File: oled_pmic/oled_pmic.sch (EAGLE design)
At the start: 11 parts, among them J1 I_sense, J2 VCC, J4 GND, Q1 N-CHANNEL-MOSFETSOT23-3, U1 AL5801W6-7

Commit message: start oled pmic module
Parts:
- removed C1: 0.1uF, scono:CAP0603-CAP
- removed D1, D2: (no value), scono:LED0603
- removed J3: (no value), scono:CONN_03
- removed J4: GND, scono:CONN_02
- added C2, C3, C4, C5, C8: 100nF, scono:CAP0402-CAP
- added C6, C7: 18pF, scono:CAP0402-CAP
- added D3: (no value), scono:LED0603
- added D4: RED, scono:LED0603
- added J10, J6: GND, scono:CONN_02
- added J12: BURNIN, scono:BURNIN
- added J5, J9: VCC, scono:CONN_02
- added J7: UART, scono:CONN_02
- added J8: FTDI, scono:CONN_06NO_SILK_FEMALE_PTH
- added Q2, Q3, Q4: N-CHANNEL-MOSFETSOT23-3, scono:N-CHANNEL-MOSFETSOT23-3
- added R10, R11, R14, R15, R18, R19, R6, R7: 100k, scono:R-US_R0402
- added R12, R16, R8: 1.6R, scono:R-US_0603
- added R13, R17, R9: 52.5k, scono:R-US_0603
- added R3: 10k, scono:R-US_R0402
- added R4, R5: 500R, scono:R-US_R0402
- added SW1: BTN-PTS810, scono:BTN-PTS810
- added TP1: TEST_POINTTHRU, scono:TEST_POINTTHRU
- added U2: LM340MPX-5.0230, scono:LM340MPX-5.0230
- added U3: ATMEGA328P-AUR, scono:ATMEGA328P-AUR
- added U4, U5, U6: AL5801W6-7, scono:AL5801W6-7
- added Y1: 16MHz, scono:CRYSTAL_SMOL
- J1: value I_sense -> (none); device scono:CONN_02 -> scono:CONN_04
- J2: value VCC -> (none); device scono:CONN_02 -> scono:CONN_04
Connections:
- removed net BIAS: J3.2, Q1.D, R2.1, U1.BIAS
- removed net FB: J3.1, R1.2, U1.FB, U1.REXT
- removed net N$2: D1.A, D2.C
- removed net N$3: J1.1, U1.OUT
- removed net N$4: D1.C, J1.2
- removed net PWM: J3.3, Q1.G
- new net 5V: C3.2, C4.2, C5.2, J12.VCC, J8.4, R3.2, R5.1, TP1.P$1, U2.5V, U3.AVCC, U3.VCC
- new net ADC0: R6.1, R7.2, U3.PC0(ADC0/PCINT8)
- new net ADC1: R10.1, R11.2, U3.PC1(ADC1/PCINT9)
- new net ADC2: R14.1, R15.2, U3.PC2(ADC2/PCINT10)
- new net ADC3: R18.1, R19.2, U3.PC3(ADC3/PCINT11)
- new net BIAS1: Q1.D, R2.1, U1.BIAS
- new net BIAS2: Q2.D, R9.1, U4.BIAS
- new net BIAS3: Q3.D, R13.1, U5.BIAS
- new net BIAS4: Q4.D, R17.1, U6.BIAS
- new net CAT1: J2.1, R6.2, U1.OUT
- new net CAT2: J2.2, R10.2, U4.OUT
- new net CAT3: J2.3, R14.2, U5.OUT
- new net CAT4: J2.4, R18.2, U6.OUT
- new net CTS: J8.5
- new net FB1: R1.2, U1.FB, U1.REXT
- new net FB2: R8.2, U4.FB, U4.REXT
- new net FB3: R12.2, U5.FB, U5.REXT
- new net FB4: R16.2, U6.FB, U6.REXT
- new net GPIO0: R4.2, U3.PD2(INT0/PCINT18)
- new net GPIO1: U3.PD3(PCINT19/OC2B/INT1)
- new net GPIO2: U3.PD4(PCINT20/XCK/T0)
- new net GPIO3: U3.PD5(PCINT21/OC0B/T1)
- new net GPIO4: U3.PD6(PCINT22/OC0A/AIN0)
- new net GPIO5: U3.PD7(PCINT23/AIN1)
- new net GPIO6: U3.PB0(PCINT0/CLKO/ICP1)
- new net GPIO7: U3.PB1(PCINT1/OC1A)
- new net MISO: J12.MISO, U3.PB4(PCINT4/MISO)
- new net MOSI: J12.MOSI, U3.PB3(PCINT3/OC2A/MOSI)
- new net N$1: D3.A, R4.1
- new net N$5: D4.A, R5.2
- new net N$6: C8.2, J8.1
- new net PWM1: Q1.G
- new net PWM2: Q2.G
- new net PWM3: Q3.G
- new net PWM4: Q4.G
- new net RST: C8.1, J12.RST, R3.1, SW1.B, U3.PC6(!RESET!/PCINT14)
- new net RX: J7.1, J8.3, U3.PD0(RXD/PCINT16)
- new net SCK: J12.SCK, U3.PB5(SCK/PCINT5)
- new net SCL: U3.PC5(ADC5/SCL/PCINT13)
- new net SDA: U3.PC4(ADC4/SDA/PCINT12)
- new net SS: U3.PB2(PCINT2/!SS!/OC1B)
- new net TX: J7.2, J8.2, U3.PD1(TXD/PCINT17)
- new net XTAL1: C6.1, U3.PB6(PCINT6/XTAL1/TOSC1), Y1.B
- new net XTAL2: C7.1, U3.PB7(PCINT7/XTAL2/TOSC2), Y1.A
- net GND: now also C2.1, C3.1, C4.1, C5.1, C6.2, C7.2, D3.C, D4.C, J10.1, J10.2, J12.GND, J6.1, J6.2, J8.6, Q2.S@2, Q3.S@2, Q4.S@2, R11.1, R12.1, R15.1, R16.1, R19.1, R7.1, R8.1, SW1.A, U2.GND, U3.GND, U4.GND, U5.GND, U6.GND; no longer C1.1, J4.1, J4.2
- net VCC: now also C2.2, J1.1, J1.2, J1.3, J1.4, J5.1, J5.2, J9.1, J9.2, R13.2, R17.2, R9.2, U2.VIN; no longer C1.2, D2.A, J2.1, J2.2

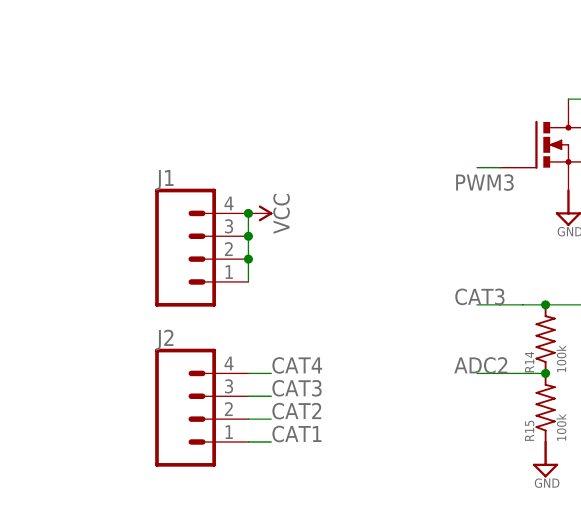
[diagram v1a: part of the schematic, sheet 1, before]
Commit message: finish oled module
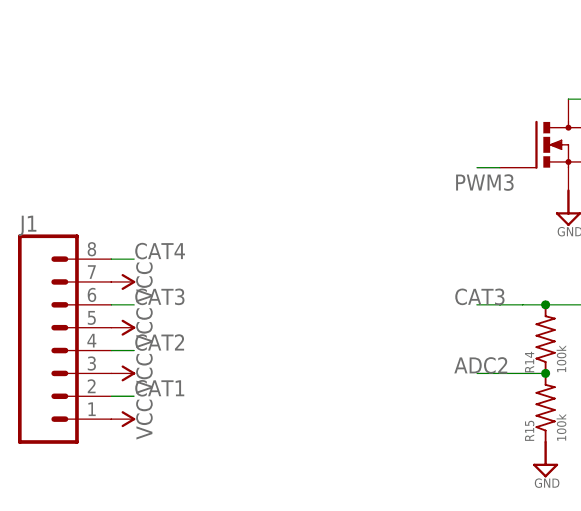
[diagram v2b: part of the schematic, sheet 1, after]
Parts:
- removed J2: (no value), scono:CONN_04
- J1: device scono:CONN_04 -> scono:CONN_08"
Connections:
- removed net GPIO1: U3.PD3(PCINT19/OC2B/INT1)
- removed net GPIO3: U3.PD5(PCINT21/OC0B/T1)
- removed net GPIO4: U3.PD6(PCINT22/OC0A/AIN0)
- removed net GPIO7: U3.PB1(PCINT1/OC1A)
- net CAT1: now also J1.2; no longer J2.1
- net CAT2: now also J1.4; no longer J2.2
- net CAT3: now also J1.6; no longer J2.3
- net CAT4: now also J1.8; no longer J2.4
- net PWM1: now also U3.PB1(PCINT1/OC1A)
- net PWM2: now also U3.PD6(PCINT22/OC0A/AIN0)
- net PWM3: now also U3.PD5(PCINT21/OC0B/T1)
- net PWM4: now also U3.PD3(PCINT19/OC2B/INT1)
- net VCC: now also J1.5, J1.7; no longer J1.2, J1.4
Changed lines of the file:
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@@
 <part name="SUPPLY24" library="scono" library_urn="urn:adsk.eagle:library:14850048" deviceset="GND" device=""/>
 <part name="TP1" library="scono" library_urn="urn:adsk.eagle:library:14850048" deviceset="TEST_POINT" device="THRU" package3d_urn="urn:adsk.eagle:package:14850798/1"/>
-<part name="J1" library="scono" library_urn="urn:adsk.eagle:library:14850048" deviceset="CONN_04" device="" package3d_urn="urn:adsk.eagle:package:38085/1"/>
-<part name="SUPPLY1" library="scono" library_urn="urn:adsk.eagle:library:14850048" deviceset="VCC" device=""/>
 <part name="R6" library="scono" library_urn="urn:adsk.eagle:library:14850048" deviceset="R-US_" device="R0402" package3d_urn="urn:adsk.eagle:package:14850590/3" value="100k"/>
 <part name="R7" library="scono" library_urn="urn:adsk.eagle:library:14850048" deviceset="R-US_" device="R0402" package3d_urn="urn:adsk.eagle:package:14850590/3" value="100k"/>
@@
 <part name="R19" library="scono" library_urn="urn:adsk.eagle:library:14850048" deviceset="R-US_" device="R0402" package3d_urn="urn:adsk.eagle:package:14850590/3" value="100k"/>
 <part name="SUPPLY33" library="scono" library_urn="urn:adsk.eagle:library:14850048" deviceset="GND" device=""/>
-<part name="J2" library="scono" library_urn="urn:adsk.eagle:library:14850048" deviceset="CONN_04" device="" package3d_urn="urn:adsk.eagle:package:38085/1"/>
+<part name="SUPPLY1" library="scono" library_urn="urn:adsk.eagle:library:14850048" deviceset="VCC" device=""/>
+<part name="SUPPLY34" library="scono" library_urn="urn:adsk.eagle:library:14850048" deviceset="VCC" device=""/>
+<part name="SUPPLY35" library="scono" library_urn="urn:adsk.eagle:library:14850048" deviceset="VCC" device=""/>
+<part name="SUPPLY36" library="scono" library_urn="urn:adsk.eagle:library:14850048" deviceset="VCC" device=""/>
+<part name="J1" library="scono" library_urn="urn:adsk.eagle:library:14850048" deviceset="CONN_08" device="&quot;" package3d_urn="urn:adsk.eagle:package:38138/1"/>
 </parts>
 <sheets>
@@
 <attribute name="VALUE" x="29.21" y="132.08" size="1.016" layer="96"/>
 </instance>
-<instance part="J1" gate="G$1" x="35.56" y="68.58" smashed="yes">
-<attribute name="VALUE" x="30.48" y="61.214" size="1.778" layer="96" font="vector"/>
-<attribute name="NAME" x="30.48" y="76.708" size="1.778" layer="95" font="vector"/>
-</instance>
-<instance part="SUPPLY1" gate="G$1" x="40.64" y="73.66" smashed="yes" rot="R270">
-<attribute name="VALUE" x="43.434" y="73.66" size="1.778" layer="96" rot="R270" align="bottom-center"/>
-</instance>
 <instance part="R6" gate="G$1" x="27.94" y="121.92" smashed="yes" rot="R90">
 <attribute name="NAME" x="26.67" y="116.84" size="1.016" layer="95" rot="R90"/>
@@
 <attribute name="VALUE" x="156.21" y="43.18" size="1.016" layer="96"/>
 </instance>
-<instance part="J2" gate="G$1" x="35.56" y="50.8" smashed="yes">
-<attribute name="VALUE" x="30.48" y="43.434" size="1.778" layer="96" font="vector"/>
-<attribute name="NAME" x="30.48" y="58.928" size="1.778" layer="95" font="vector"/>
+<instance part="SUPPLY1" gate="G$1" x="25.4" y="66.04" smashed="yes" rot="R270">
+<attribute name="VALUE" x="28.194" y="66.04" size="1.778" layer="96" rot="R270" align="bottom-center"/>
+</instance>
+<instance part="SUPPLY34" gate="G$1" x="25.4" y="60.96" smashed="yes" rot="R270">
+<attribute name="VALUE" x="28.194" y="60.96" size="1.778" layer="96" rot="R270" align="bottom-center"/>
+</instance>
+<instance part="SUPPLY35" gate="G$1" x="25.4" y="55.88" smashed="yes" rot="R270">
+<attribute name="VALUE" x="28.194" y="55.88" size="1.778" layer="96" rot="R270" align="bottom-center"/>
+</instance>
+<instance part="SUPPLY36" gate="G$1" x="25.4" y="50.8" smashed="yes" rot="R270">
+<attribute name="VALUE" x="28.194" y="50.8" size="1.778" layer="96" rot="R270" align="bottom-center"/>
+</instance>
+<instance part="J1" gate="G$1" x="20.32" y="58.42" smashed="yes">
+<attribute name="VALUE" x="15.24" y="45.974" size="1.778" layer="96" font="vector"/>
+<attribute name="NAME" x="15.24" y="71.628" size="1.778" layer="95" font="vector"/>
 </instance>
 </instances>
@@
 </segment>
 <segment>
-<pinref part="J1" gate="G$1" pin="4"/>
-<pinref part="SUPPLY1" gate="G$1" pin="VCC"/>
-<pinref part="J1" gate="G$1" pin="3"/>
-<wire x1="40.64" y1="73.66" x2="40.64" y2="71.12" width="0.1524" layer="91"/>
-<junction x="40.64" y="73.66"/>
-<pinref part="J1" gate="G$1" pin="2"/>
-<wire x1="40.64" y1="71.12" x2="40.64" y2="68.58" width="0.1524" layer="91"/>
-<junction x="40.64" y="71.12"/>
-<pinref part="J1" gate="G$1" pin="1"/>
-<wire x1="40.64" y1="68.58" x2="40.64" y2="66.04" width="0.1524" layer="91"/>
-<junction x="40.64" y="68.58"/>
-</segment>
-<segment>
 <pinref part="R9" gate="G$1" pin="2"/>
 <pinref part="SUPPLY5" gate="G$1" pin="VCC"/>
@@
 <pinref part="R17" gate="G$1" pin="2"/>
 <pinref part="SUPPLY30" gate="G$1" pin="VCC"/>
+</segment>
+<segment>
+<pinref part="SUPPLY1" gate="G$1" pin="VCC"/>
+<pinref part="J1" gate="G$1" pin="7"/>
+</segment>
+<segment>
+<pinref part="SUPPLY34" gate="G$1" pin="VCC"/>
+<pinref part="J1" gate="G$1" pin="5"/>
+</segment>
+<segment>
+<pinref part="SUPPLY35" gate="G$1" pin="VCC"/>
+<pinref part="J1" gate="G$1" pin="3"/>
+</segment>
+<segment>
+<pinref part="SUPPLY36" gate="G$1" pin="VCC"/>
+<pinref part="J1" gate="G$1" pin="1"/>
 </segment>
 </net>
@@
 </segment>
 <segment>
-<pinref part="J2" gate="G$1" pin="1"/>
-<wire x1="40.64" y1="48.26" x2="43.18" y2="48.26" width="0.1524" layer="91"/>
-<label x="43.18" y="48.26" size="1.778" layer="95"/>
+<wire x1="25.4" y1="53.34" x2="27.94" y2="53.34" width="0.1524" layer="91"/>
+<label x="27.94" y="53.34" size="1.778" layer="95"/>
+<pinref part="J1" gate="G$1" pin="2"/>
 </segment>
 </net>
@@
 </segment>
 <segment>
-<pinref part="J2" gate="G$1" pin="2"/>
-<wire x1="40.64" y1="50.8" x2="43.18" y2="50.8" width="0.1524" layer="91"/>
-<label x="43.18" y="50.8" size="1.778" layer="95"/>
+<wire x1="25.4" y1="58.42" x2="27.94" y2="58.42" width="0.1524" layer="91"/>
+<label x="27.94" y="58.42" size="1.778" layer="95"/>
+<pinref part="J1" gate="G$1" pin="4"/>
 </segment>
 </net>
@@
 </segment>
 <segment>
-<pinref part="J2" gate="G$1" pin="3"/>
-<wire x1="40.64" y1="53.34" x2="43.18" y2="53.34" width="0.1524" layer="91"/>
-<label x="43.18" y="53.34" size="1.778" layer="95"/>
+<wire x1="25.4" y1="63.5" x2="27.94" y2="63.5" width="0.1524" layer="91"/>
+<label x="27.94" y="63.5" size="1.778" layer="95"/>
+<pinref part="J1" gate="G$1" pin="6"/>
 </segment>
 </net>
@@
 </segment>
 <segment>
-<pinref part="J2" gate="G$1" pin="4"/>
-<wire x1="40.64" y1="55.88" x2="43.18" y2="55.88" width="0.1524" layer="91"/>
-<label x="43.18" y="55.88" size="1.778" layer="95"/>
+<wire x1="25.4" y1="68.58" x2="27.94" y2="68.58" width="0.1524" layer="91"/>
+<label x="27.94" y="68.58" size="1.778" layer="95"/>
+<pinref part="J1" gate="G$1" pin="8"/>
 </segment>
 </net>
@@
 </segment>
 </net>
-<net name="GPIO1" class="0">
+<net name="PWM4" class="0">
 <segment>
 <pinref part="U3" gate="G$1" pin="PD3(PCINT19/OC2B/INT1)"/>
@@
 </segment>
 </net>
-<net name="GPIO3" class="0">
+<net name="PWM3" class="0">
 <segment>
 <pinref part="U3" gate="G$1" pin="PD5(PCINT21/OC0B/T1)"/>
@@
 </segment>
 </net>
-<net name="GPIO4" class="0">
+<net name="PWM2" class="0">
 <segment>
 <pinref part="U3" gate="G$1" pin="PD6(PCINT22/OC0A/AIN0)"/>
@@
 </segment>
 </net>
-<net name="GPIO7" class="0">
+<net name="PWM1" class="0">
 <segment>
 <pinref part="U3" gate="G$1" pin="PB1(PCINT1/OC1A)"/>
